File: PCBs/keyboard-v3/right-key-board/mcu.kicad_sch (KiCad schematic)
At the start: 5 parts, among them J301 F31Z1A7H111008, U301 STM32G0C1CEUx

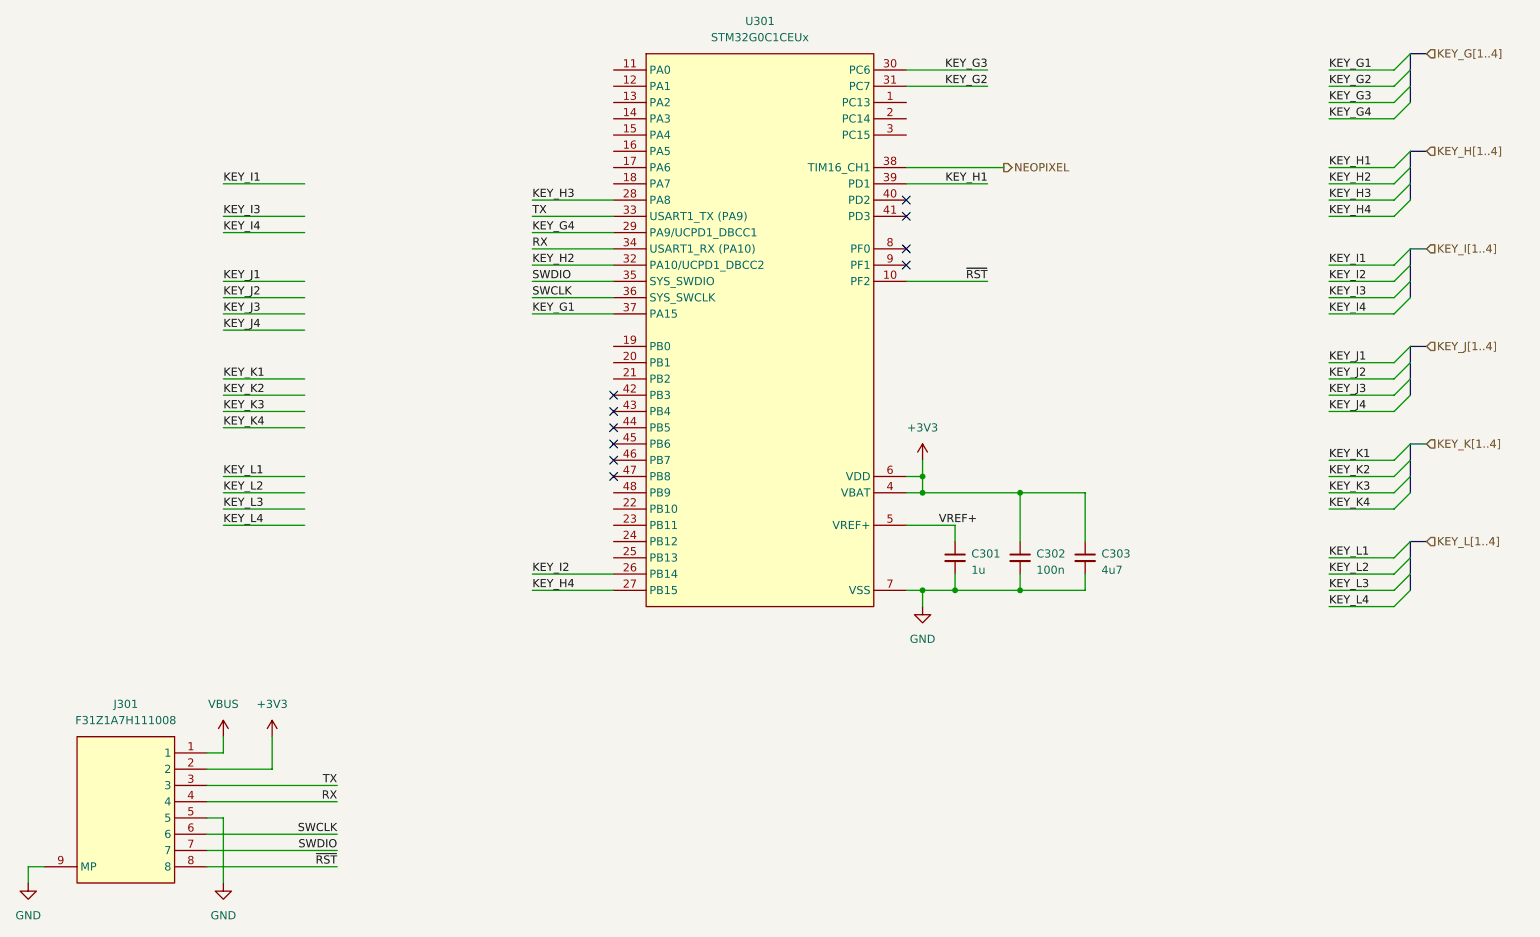
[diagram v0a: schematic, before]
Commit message: Right daughter boards finished
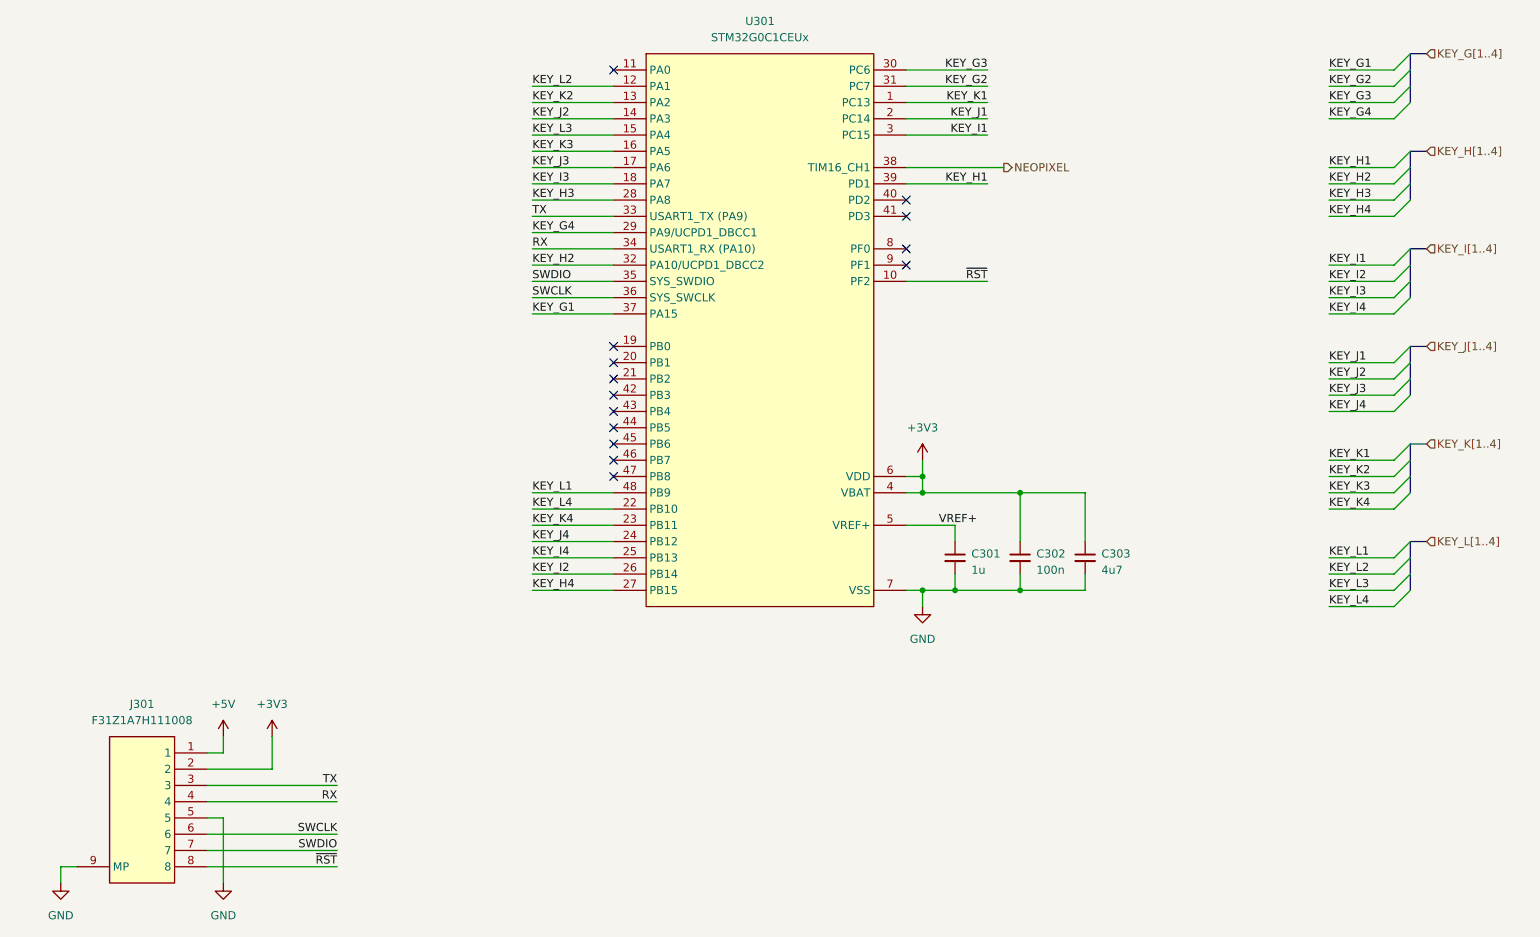
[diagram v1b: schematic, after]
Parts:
- J301: symbol CONN-FPC:F31Z1A7H111008 -> CONN-FPC:F31Z-1A7H1-11008
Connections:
- net KEY_I1: now also U301.3 (PC15)
- net KEY_I3: now also U301.18 (PA7)
- net KEY_I4: now also U301.25 (PB13)
- net KEY_J1: now also U301.2 (PC14)
- net KEY_J2: now also U301.14 (PA3)
- net KEY_J3: now also U301.17 (PA6)
- net KEY_J4: now also U301.24 (PB12)
- net KEY_K1: now also U301.1 (PC13)
- net KEY_K2: now also U301.13 (PA2)
- net KEY_K3: now also U301.16 (PA5)
- net KEY_K4: now also U301.23 (PB11)
- net KEY_L1: now also U301.48 (PB9)
- net KEY_L2: now also U301.12 (PA1)
- net KEY_L3: now also U301.15 (PA4)
- net KEY_L4: now also U301.22 (PB10)
- net VBUS renamed +5V
- no-connect marks 10 -> 14
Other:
- moved on the sheet: J301
